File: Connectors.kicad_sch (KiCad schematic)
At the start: 0 parts

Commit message: Added symbol for ATMEGA328P-AU
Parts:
- added J1: Conn_01x09, symbol Connector_Generic:Conn_01x09
- added J2, J4: Conn_01x04, symbol Connector_Generic:Conn_01x04
- added J3: Conn_02x03_Odd_Even, symbol Connector_Generic:Conn_02x03_Odd_Even

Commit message: Arranged symbols
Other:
- moved on the sheet: J1, J2, J3, J4
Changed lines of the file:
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@@
 	(symbol
 		(lib_id "Connector_Generic:Conn_02x03_Odd_Even")
-		(at 97.79 90.17 0)
+		(at 120.65 113.03 0)
 		(unit 1)
 		(exclude_from_sim no)
@@
 		(fields_autoplaced yes)
 		(property "Reference" "J3"
-			(at 99.06 81.28 0)
+			(at 121.92 104.14 0)
 			(effects
 				(font
@@
 		)
 		(property "Value" "Conn_02x03_Odd_Even"
-			(at 99.06 83.82 0)
-			(effects
-				(font
-					(size 1.27 1.27)
-				)
-			)
-		)
-		(property "Footprint" ""
-			(at 97.79 90.17 0)
-			(effects
-				(font
-					(size 1.27 1.27)
-				)
-				(hide yes)
-			)
-		)
-		(property "Datasheet" "~"
-			(at 97.79 90.17 0)
+			(at 121.92 106.68 0)
+			(effects
+				(font
+					(size 1.27 1.27)
+				)
+			)
+		)
+		(property "Footprint" ""
+			(at 120.65 113.03 0)
+			(effects
+				(font
+					(size 1.27 1.27)
+				)
+				(hide yes)
+			)
+		)
+		(property "Datasheet" "~"
+			(at 120.65 113.03 0)
 			(effects
 				(font
@@
 		)
 		(property "Description" "Generic connector, double row, 02x03, odd/even pin numbering scheme (row 1 odd numbers, row 2 even numbers), script generated (kicad-library-utils/schlib/autogen/connector/)"
-			(at 97.79 90.17 0)
+			(at 120.65 113.03 0)
 			(effects
 				(font
@@
 	(symbol
 		(lib_id "Connector_Generic:Conn_01x04")
-		(at 97.79 68.58 0)
+		(at 157.48 80.01 0)
 		(unit 1)
 		(exclude_from_sim no)
@@
 		(fields_autoplaced yes)
 		(property "Reference" "J2"
-			(at 100.33 68.5799 0)
+			(at 160.02 80.0099 0)
 			(effects
 				(font
@@
 		)
 		(property "Value" "Conn_01x04"
-			(at 100.33 71.1199 0)
-			(effects
-				(font
-					(size 1.27 1.27)
-				)
-				(justify left)
-			)
-		)
-		(property "Footprint" ""
-			(at 97.79 68.58 0)
-			(effects
-				(font
-					(size 1.27 1.27)
-				)
-				(hide yes)
-			)
-		)
-		(property "Datasheet" "~"
-			(at 97.79 68.58 0)
+			(at 160.02 82.5499 0)
+			(effects
+				(font
+					(size 1.27 1.27)
+				)
+				(justify left)
+			)
+		)
+		(property "Footprint" ""
+			(at 157.48 80.01 0)
+			(effects
+				(font
+					(size 1.27 1.27)
+				)
+				(hide yes)
+			)
+		)
+		(property "Datasheet" "~"
+			(at 157.48 80.01 0)
 			(effects
 				(font
@@
 		)
 		(property "Description" "Generic connector, single row, 01x04, script generated (kicad-library-utils/schlib/autogen/connector/)"
-			(at 97.79 68.58 0)
+			(at 157.48 80.01 0)
 			(effects
 				(font
@@
 	(symbol
 		(lib_id "Connector_Generic:Conn_01x09")
-		(at 62.23 78.74 0)
+		(at 120.65 80.01 0)
 		(unit 1)
 		(exclude_from_sim no)
@@
 		(fields_autoplaced yes)
 		(property "Reference" "J1"
-			(at 64.77 77.4699 0)
+			(at 123.19 78.7399 0)
 			(effects
 				(font
@@
 		)
 		(property "Value" "Conn_01x09"
-			(at 64.77 80.0099 0)
-			(effects
-				(font
-					(size 1.27 1.27)
-				)
-				(justify left)
-			)
-		)
-		(property "Footprint" ""
-			(at 62.23 78.74 0)
-			(effects
-				(font
-					(size 1.27 1.27)
-				)
-				(hide yes)
-			)
-		)
-		(property "Datasheet" "~"
-			(at 62.23 78.74 0)
+			(at 123.19 81.2799 0)
+			(effects
+				(font
+					(size 1.27 1.27)
+				)
+				(justify left)
+			)
+		)
+		(property "Footprint" ""
+			(at 120.65 80.01 0)
+			(effects
+				(font
+					(size 1.27 1.27)
+				)
+				(hide yes)
+			)
+		)
+		(property "Datasheet" "~"
+			(at 120.65 80.01 0)
 			(effects
 				(font
@@
 		)
 		(property "Description" "Generic connector, single row, 01x09, script generated (kicad-library-utils/schlib/autogen/connector/)"
-			(at 62.23 78.74 0)
+			(at 120.65 80.01 0)
 			(effects
 				(font
@@
 	(symbol
 		(lib_id "Connector_Generic:Conn_01x04")
-		(at 121.92 91.44 0)
+		(at 157.48 111.76 0)
 		(unit 1)
 		(exclude_from_sim no)
@@
 		(fields_autoplaced yes)
 		(property "Reference" "J4"
-			(at 124.46 91.4399 0)
+			(at 160.02 111.7599 0)
 			(effects
 				(font
@@
 		)
 		(property "Value" "Conn_01x04"
-			(at 124.46 93.9799 0)
-			(effects
-				(font
-					(size 1.27 1.27)
-				)
-				(justify left)
-			)
-		)
-		(property "Footprint" ""
-			(at 121.92 91.44 0)
-			(effects
-				(font
-					(size 1.27 1.27)
-				)
-				(hide yes)
-			)
-		)
-		(property "Datasheet" "~"
-			(at 121.92 91.44 0)
+			(at 160.02 114.2999 0)
+			(effects
+				(font
+					(size 1.27 1.27)
+				)
+				(justify left)
+			)
+		)
+		(property "Footprint" ""
+			(at 157.48 111.76 0)
+			(effects
+				(font
+					(size 1.27 1.27)
+				)
+				(hide yes)
+			)
+		)
+		(property "Datasheet" "~"
+			(at 157.48 111.76 0)
 			(effects
 				(font
@@
 		)
 		(property "Description" "Generic connector, single row, 01x04, script generated (kicad-library-utils/schlib/autogen/connector/)"
-			(at 121.92 91.44 0)
-			(effects
-				(font
+			(at 157.48 111.76 0)
+			(effects
+				(font

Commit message: Assigned the footprints
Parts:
- J1: footprint (none) -> Connector_PinSocket_2.54mm:PinSocket_1x09_P2.54mm_Vertical
- J2, J4: footprint (none) -> Connector_PinSocket_2.54mm:PinSocket_1x04_P2.54mm_Vertical
- J3: footprint (none) -> Connector_PinSocket_2.54mm:PinSocket_2x03_P2.54mm_Vertical
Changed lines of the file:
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@@
 			)
 		)
-		(property "Footprint" ""
+		(property "Footprint" "Connector_PinSocket_2.54mm:PinSocket_2x03_P2.54mm_Vertical"
 			(at 120.65 113.03 0)
 			(effects
@@
 			)
 		)
-		(property "Footprint" ""
+		(property "Footprint" "Connector_PinSocket_2.54mm:PinSocket_1x04_P2.54mm_Vertical"
 			(at 157.48 80.01 0)
 			(effects
@@
 			)
 		)
-		(property "Footprint" ""
+		(property "Footprint" "Connector_PinSocket_2.54mm:PinSocket_1x09_P2.54mm_Vertical"
 			(at 120.65 80.01 0)
 			(effects
@@
 			)
 		)
-		(property "Footprint" ""
+		(property "Footprint" "Connector_PinSocket_2.54mm:PinSocket_1x04_P2.54mm_Vertical"
 			(at 157.48 111.76 0)
 			(effects

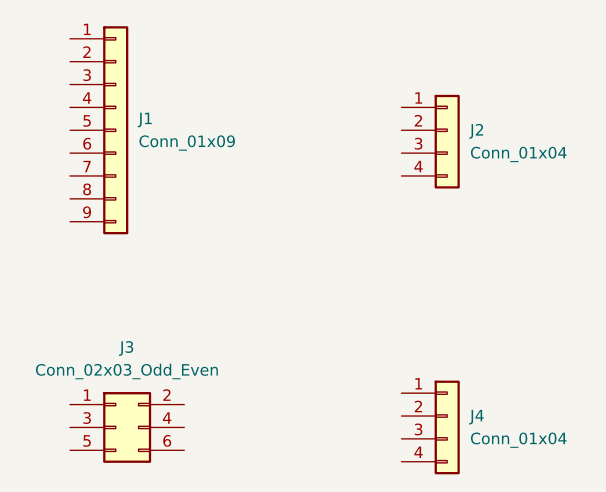
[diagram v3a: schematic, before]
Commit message: Completed adding components values
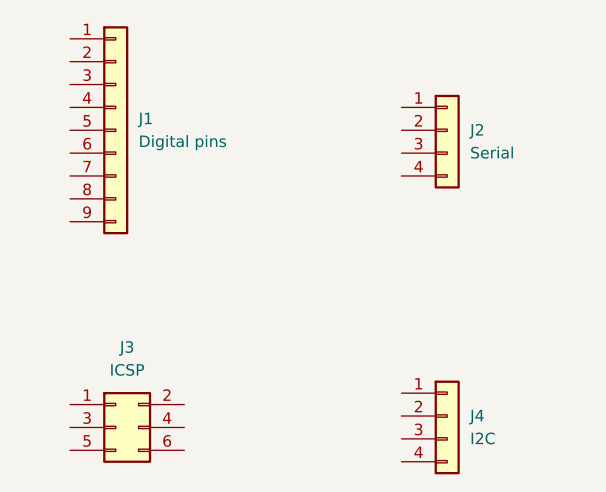
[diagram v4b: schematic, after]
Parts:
- J1: value Conn_01x09 -> Digital pins
- J2: value Conn_01x04 -> Serial
- J3: value Conn_02x03_Odd_Even -> ICSP
- J4: value Conn_01x04 -> I2C
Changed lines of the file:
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@@
 			)
 		)
-		(property "Value" "Conn_02x03_Odd_Even"
+		(property "Value" "ICSP"
 			(at 121.92 106.68 0)
 			(effects
@@
 			)
 		)
-		(property "Value" "Conn_01x04"
+		(property "Value" "Serial"
 			(at 160.02 82.5499 0)
 			(effects
@@
 			)
 		)
-		(property "Value" "Conn_01x09"
+		(property "Value" "Digital pins"
 			(at 123.19 81.2799 0)
 			(effects
@@
 			)
 		)
-		(property "Value" "Conn_01x04"
+		(property "Value" "I2C"
 			(at 160.02 114.2999 0)
 			(effects

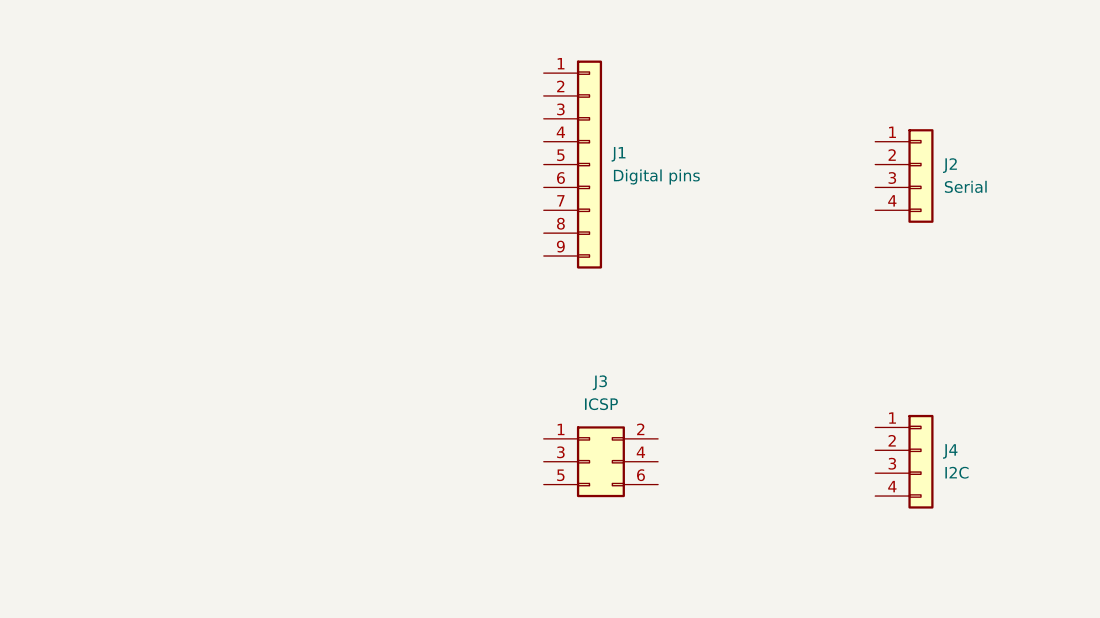
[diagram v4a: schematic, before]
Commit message: Completed wiring in child sheet
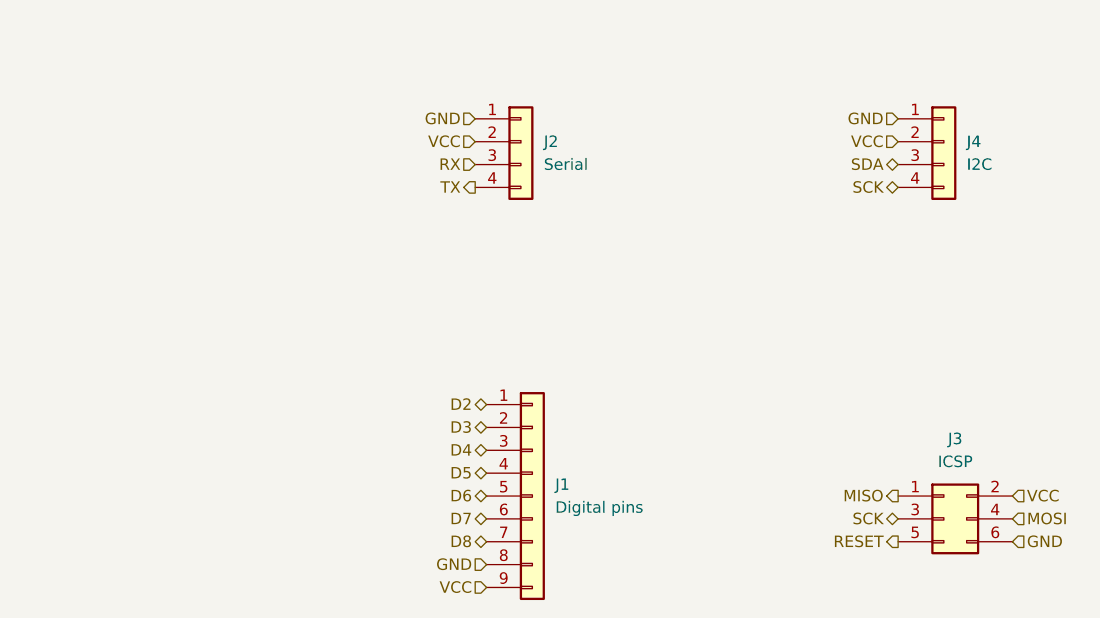
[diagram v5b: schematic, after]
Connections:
- net MISO: now reaches J3.1 (Pin_1)
- net VCC: now reaches J3.2 (Pin_2)
- net VCC: now also J1.9 (Pin_9), J2.2 (Pin_2), J4.2 (Pin_2)
- net SCK: now reaches J3.3 (Pin_3)
- net SCK: now also J4.4 (Pin_4)
- net MOSI: now reaches J3.4 (Pin_4)
- net RESET: now reaches J3.5 (Pin_5)
- net GND: now reaches J3.6 (Pin_6)
- net GND: now also J1.8 (Pin_8), J2.1 (Pin_1), J4.1 (Pin_1)
- net RX: now reaches J2.3 (Pin_3)
- net TX: now reaches J2.4 (Pin_4)
- net D2: now reaches J1.1 (Pin_1)
- net D3: now reaches J1.2 (Pin_2)
- net D4: now reaches J1.3 (Pin_3)
- net D5: now reaches J1.4 (Pin_4)
- net D6: now reaches J1.5 (Pin_5)
- net D7: now reaches J1.6 (Pin_6)
- net D8: now reaches J1.7 (Pin_7)
- net SDA: now reaches J4.3 (Pin_3)
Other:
- moved on the sheet: J1, J2, J3, J4

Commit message: Added functional block descriptions
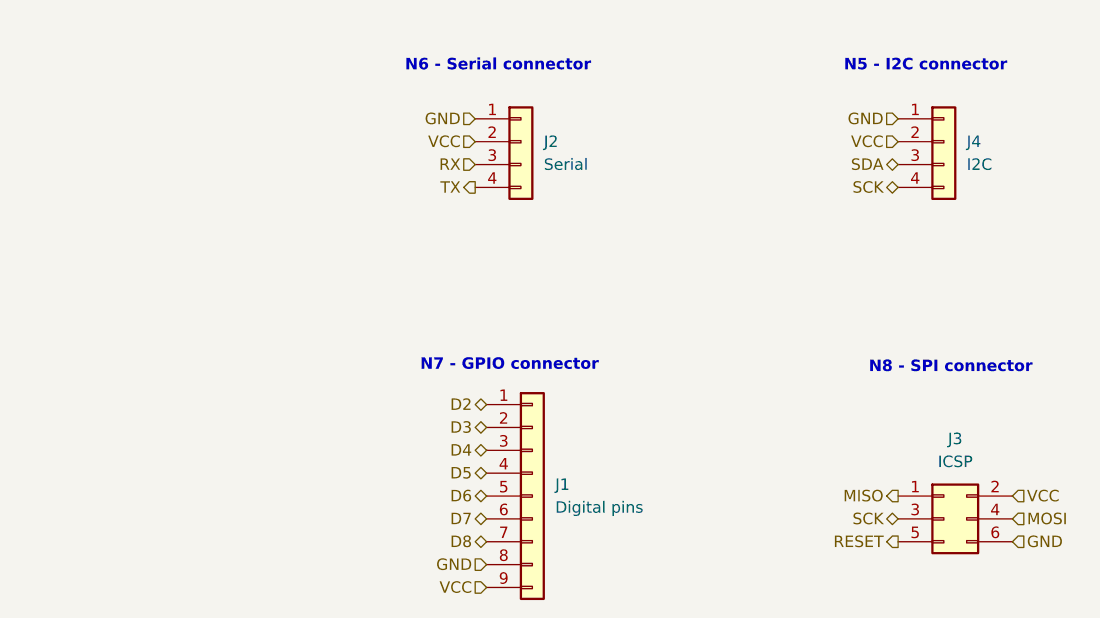
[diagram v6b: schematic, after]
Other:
- note added: "N5 - I2C connector"
- note added: "N6 - Serial connector"
- note added: "N7 - GPIO connector"
- note added: "N8 - SPI connector"
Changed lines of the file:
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@@
 		(comment 1 "Designed by Gathonjia in Toll, Nanyuki")
+	)
+	(text "N8 - SPI connector"
+		(exclude_from_sim no)
+		(at 160.782 102.616 0)
+		(effects
+			(font
+				(size 1.27 1.27)
+				(thickness 0.254)
+				(bold yes)
+			)
+		)
+	)
+	(text "N6 - Serial connector"
+		(exclude_from_sim no)
+		(at 110.49 69.088 0)
+		(effects
+			(font
+				(size 1.27 1.27)
+				(thickness 0.254)
+				(bold yes)
+			)
+		)
+	)
+	(text "N5 - I2C connector"
+		(exclude_from_sim no)
+		(at 157.988 69.088 0)
+		(effects
+			(font
+				(size 1.27 1.27)
+				(thickness 0.254)
+				(bold yes)
+			)
+		)
+	)
+	(text "N7 - GPIO connector"
+		(exclude_from_sim no)
+		(at 111.76 102.362 0)
+		(effects
+			(font
+				(size 1.27 1.27)
+				(thickness 0.254)
+				(bold yes)
+			)
+		)
 	)
 	(hierarchical_label "GND"
